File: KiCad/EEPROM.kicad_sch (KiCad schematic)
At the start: 2 parts, among them U10 24LC256

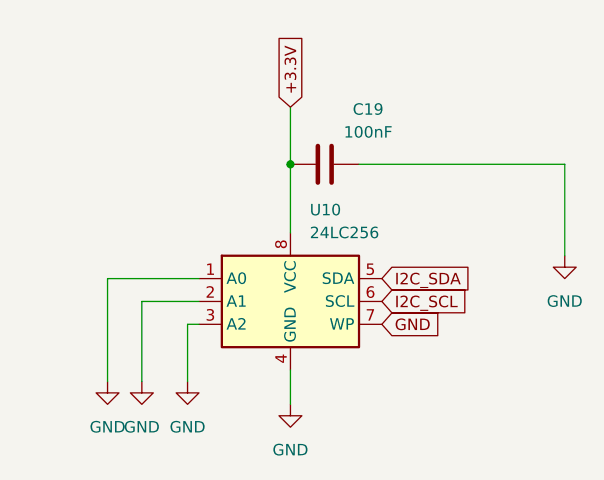
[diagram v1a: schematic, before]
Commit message: Arreglada la EEPROM
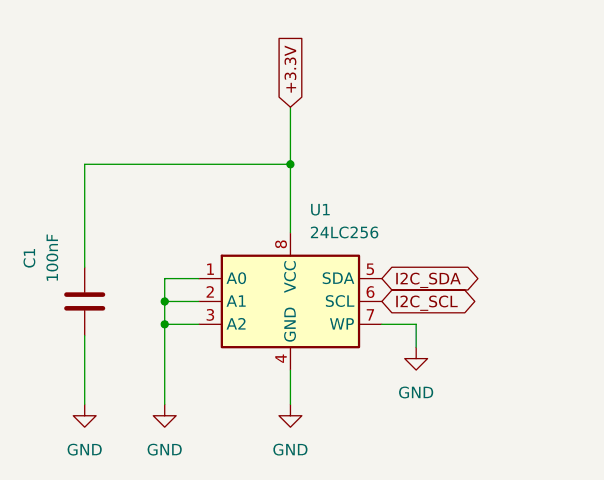
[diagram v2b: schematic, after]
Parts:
- renumbered C19 to C1, U10 to U1
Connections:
- net +3.3V: now also C1.2; no longer C1.1
- net GND: now also C1.1; no longer C1.2
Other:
- moved on the sheet: C1
